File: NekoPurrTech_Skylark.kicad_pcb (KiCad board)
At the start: 4 copper layers, 36.5 x 36.5 mm, 120 parts, among them IC1 ICM-42688-P, IC2 W25Q256JWPIQ, IC3 LP2992IM5-3.3, IC4 LP2992IM5-3.3, IC5 LP2992IM5-3.3, J1 Motor, J2 DJI_VTX, J3 GPS, J4 CRSF_Receiver, J5 Analog_Camera, J6 Conn_01x21_Pin, J7 USB_C_Receptacle, J8 Conn_01x20_Pin, Q2 SS8050, U1 STM32F405RGTx, U2 DPS310, U3 AT7456E, U4 MP9943AGQ-Z, U5 MP9943AGQ-Z, U6 74LVC1G04, U7 USBLC6-2P6, U8 SN74LV4T125RGYR, Y1 YSX321SL

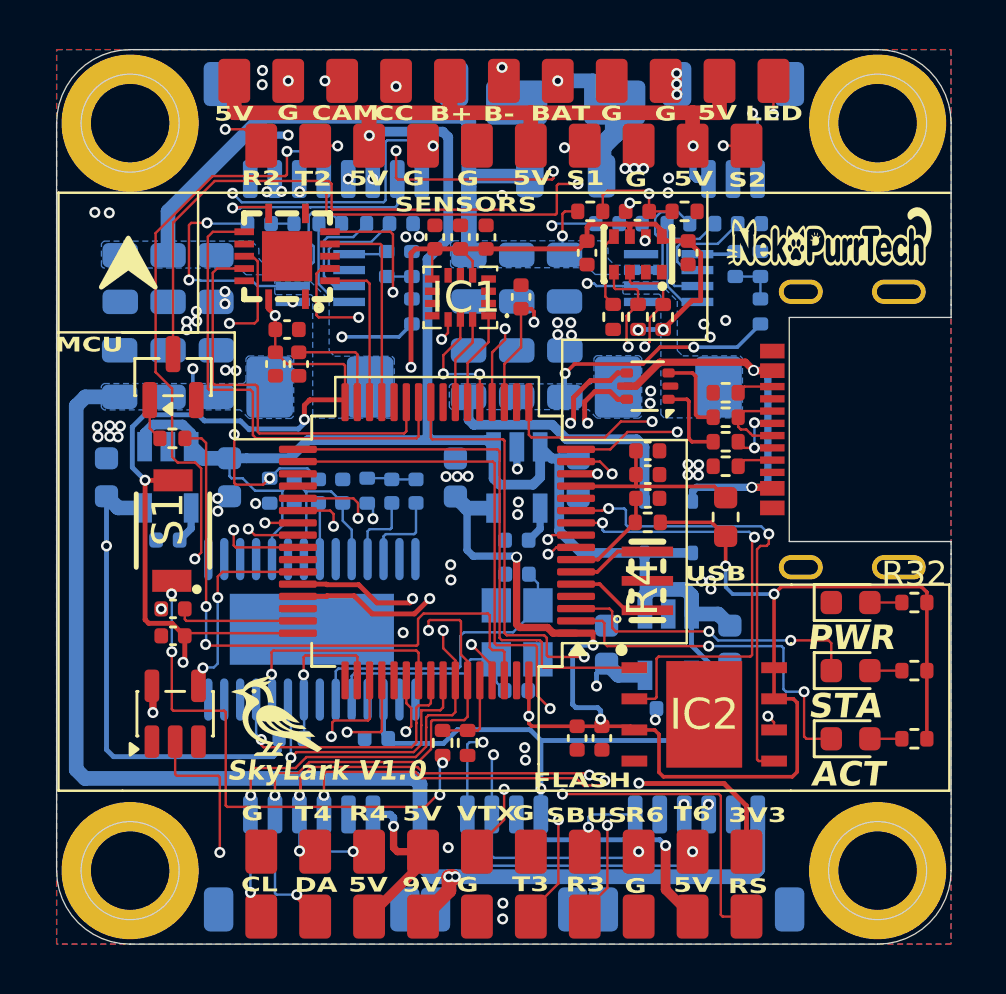
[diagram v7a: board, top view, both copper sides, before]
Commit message: Finished PCB SilkScreen V1.0
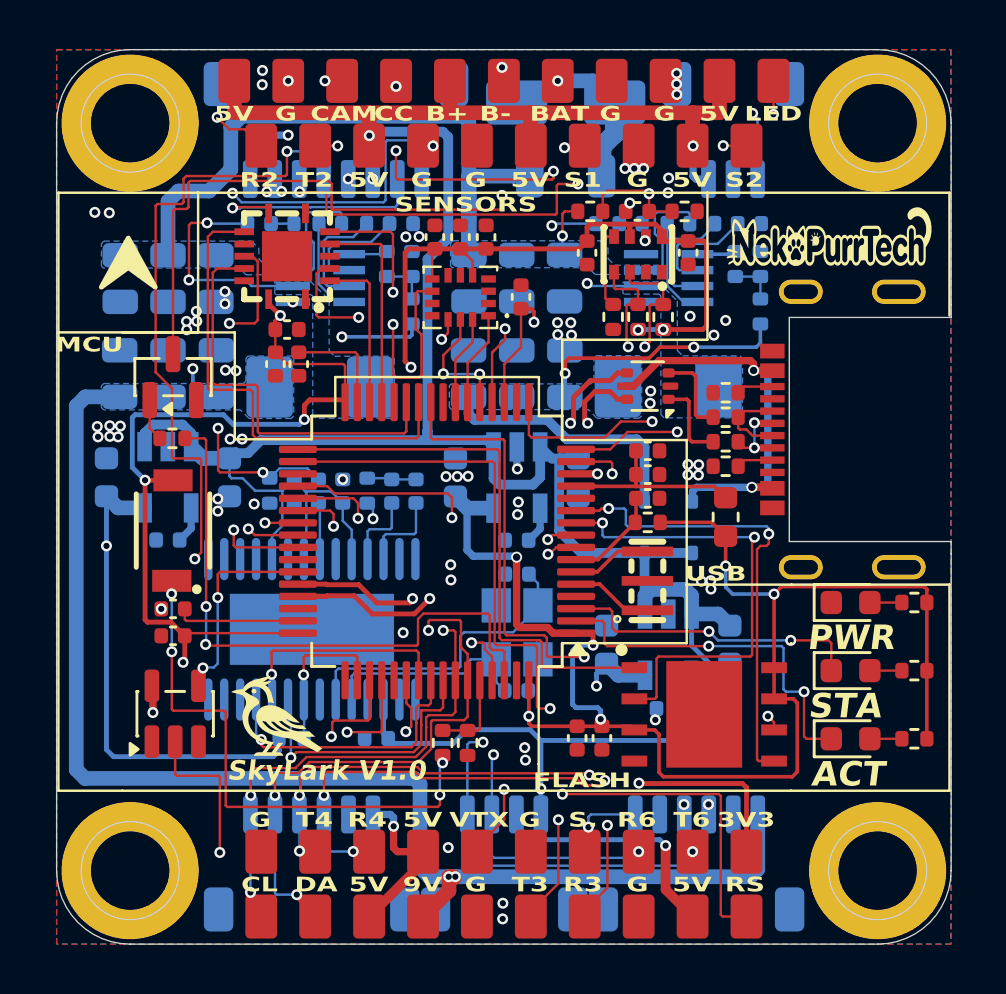
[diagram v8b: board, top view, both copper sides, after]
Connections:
- U1 pad 36: GYRO_CLK -> IMU_CLKIN
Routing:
- net IMU_CLKIN: track 0.00 -> 38.7 mm, vias 0 -> 2
- net VBAT_IN: track 41.1 -> 43.2 mm
- net +3.3V_SENSOR: track 65.5 -> 67.1 mm
- net USART2_RX: track 57.2 -> 58.8 mm
- net USART5_RX: track 42.2 -> 43.8 mm
- net VRX: track 53.9 -> 54.9 mm
- net BEEPER-: track 26.3 -> 27.2 mm
- net +3.3V_PREP: track 16.7 -> 17.6 mm
- net USART2_TX: track 48.3 -> 49.1 mm
- net CAMERA_CTRL: track 38.1 -> 38.7 mm
- net VCC_5V: track 20.6 -> 21.2 mm
- net +3.3V_MCU: track 143.7 -> 144.2 mm
- net GND: track 0.91 -> 0.96 mm, vias 66 -> 69
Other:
- board text added: "OSD"
- board text added: "POWER"
- board text added: "S."
- board text removed: "${REFERENCE}"
- board text removed: "SBUS"
